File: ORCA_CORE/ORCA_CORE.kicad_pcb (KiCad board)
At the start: 4 copper layers, 73 x 134.1 mm, 183 parts, among them J1 data_line_power, J10 Raspberry_Pi_2_3, J11 I2C, J12 I2C, J13 6Vout, J15 Conn_01x05_Pin, J16 Conn_01x05_Pin, J17 Vin_motor, J18 data_line_power, J19 +5Vin_cpu, J2 I2C_power, J20 5Vout, J21 Conn_01x02, J3 Vout_motor, J4 emergence, J5 Vin_batt, J6 Vin_ex, J7 Vout_power2usp, J8 Vin_power2usp, J9 +5Vout_cpu, P1 USB_C_Plug_USB2.0, Q1 TJ60S04M3L, Q2 BSS138, Q3 BSS138, Q4 IRLML6402, Q5 TJ60S04M3L, Q6 BSS138, Q7 BSS138, Q8 BSS138, U1 LTC2301IMS, U10 HY2112, U11 AP64502, U12 TPS61230A__board, U13 FT230XS, U14 BNO055, U15 NJM78055DL1, U2 NJM78055DL1, U3 CN3058E, U4 RH1B-UDC6V, U5 TPH11006NL, U6 TPH11006NL, U7 NJW4860, U8 AZ1117-3.3, U9 FS8205

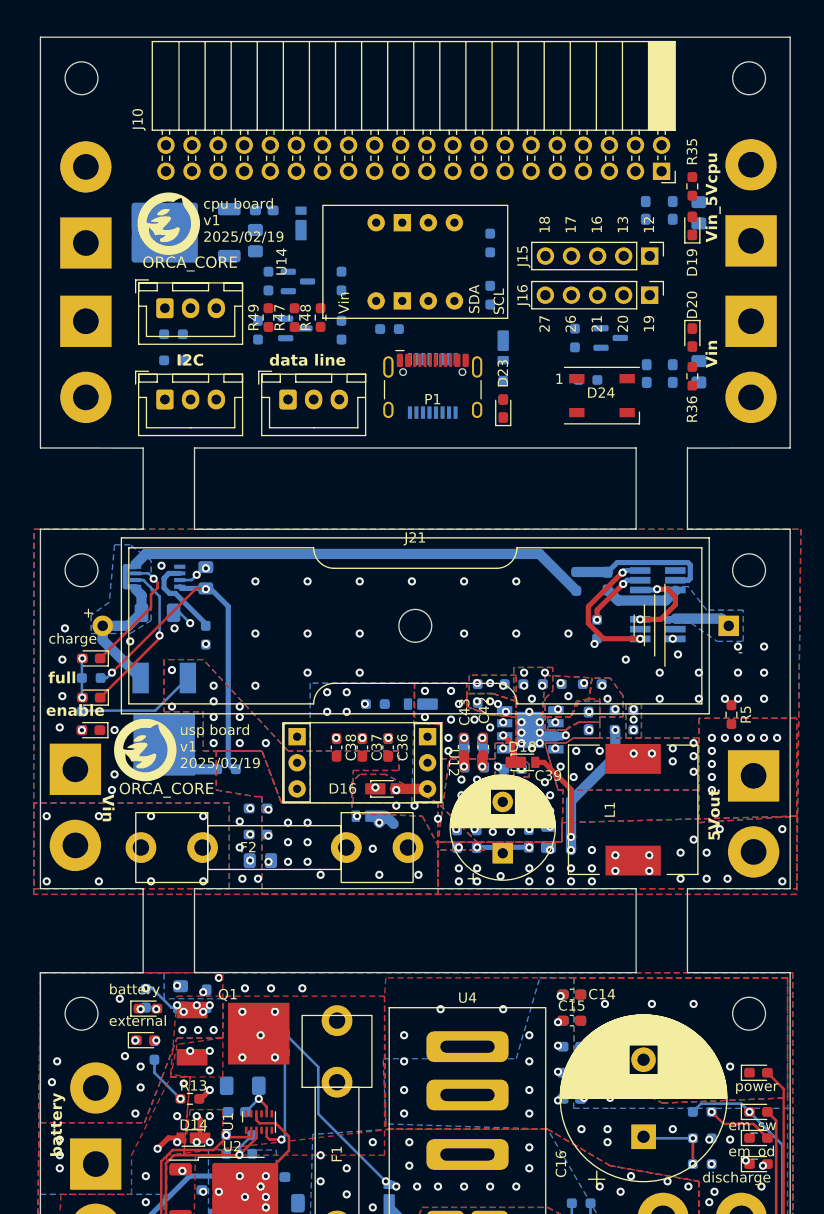
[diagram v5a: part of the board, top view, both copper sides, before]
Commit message: wired and filled all borad
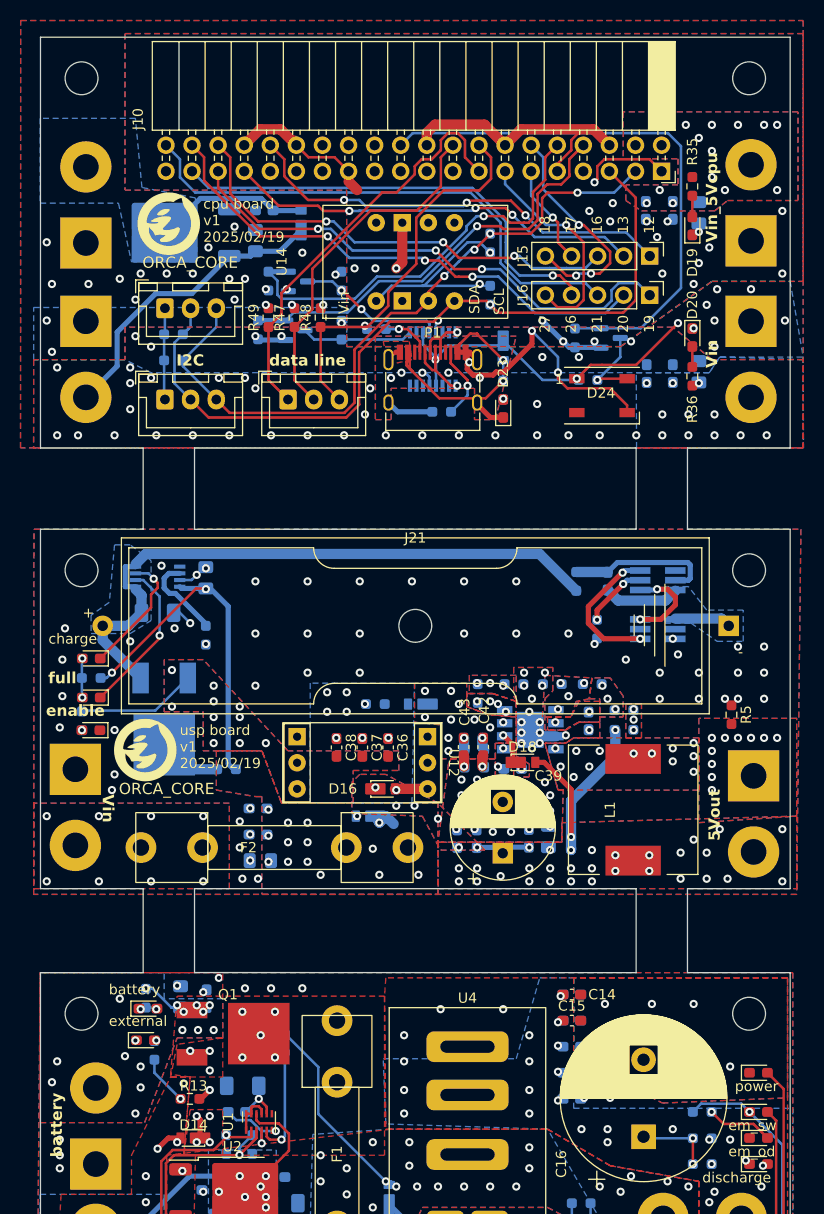
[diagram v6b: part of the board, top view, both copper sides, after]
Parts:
- added R51: 5.1k, Resistor_SMD:R_0603_1608Metric_Pad0.98x0.95mm_HandSolder, B.Cu at (132.4, 64.8)
- P1: value USB_C_Plug_USB2.0 -> USB_C_Receptacle_USB2.0; footprint Connector_USB:USB_C_Receptacle_HCTL_HC-TYPE-C-16P-01A_withmodel -> Conn:USB_C_Receptacle_XKB_U262-16XN-4BVC11
- moved U13 2.61 mm to (131.6, 59.6)
- moved R39 1.27 mm to (126.1, 56.7)
- moved P1 0.71 mm to (131.6, 62.8)
- moved Q6 0.18 mm to (118.2, 56.8)
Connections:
- D22 pad 2: Net-(D22-A) -> GND2
- P1 pad A4: Net-(D22-A) -> GND2
- P1 pad A6: Net-(P1-D+) -> Net-(U13-USBDP)
- P1 pad A7: Net-(P1-D-) -> Net-(U13-USBDM)
- P1 pad A8: (no net) -> unconnected-(P1-SBU1-PadA8)
- P1 pad A9: Net-(D22-A) -> GND2
- P1 pad B4: Net-(D22-A) -> GND2
- P1 pad B5: unconnected-(P1-VCONN-PadB5) -> Net-(P1-CC2)
- P1 pad B6: (no net) -> Net-(U13-USBDP)
- P1 pad B7: (no net) -> Net-(U13-USBDM)
- P1 pad B8: (no net) -> unconnected-(P1-SBU2-PadB8)
- P1 pad B9: Net-(D22-A) -> GND2
- R40 pad 1: Net-(D22-A) -> GND2
- U13 pad 8: Net-(P1-D+) -> Net-(U13-USBDP)
- U13 pad 9: Net-(P1-D-) -> Net-(U13-USBDM)
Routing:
- net GND2: track 0.00 -> 137.6 mm, vias 0 -> 30
- net SCL: track 0.00 -> 76.5 mm, vias 0 -> 1
- net SDA: track 0.00 -> 68.0 mm, vias 0 -> 4
- net +3V3_cpu: track 0.00 -> 58.4 mm, vias 0 -> 9
- net full_color_led_3V3: track 0.00 -> 54.1 mm
- net /cpu/GPIO21: track 0.00 -> 51.4 mm
- net /cpu/GPIO20: track 0.00 -> 50.9 mm, vias 0 -> 3
- net +5V_cpu: track 0.00 -> 50.7 mm, vias 0 -> 19
- net /cpu/GPIO19: track 0.00 -> 50.6 mm, vias 0 -> 3
- net /cpu/GPIO26: track 0.00 -> 44.7 mm, vias 0 -> 1
- net /cpu/GPIO16: track 0.00 -> 44.6 mm, vias 0 -> 3
- net /cpu/GPIO12: track 0.00 -> 43.2 mm, vias 0 -> 3
- net RXD_3V3: track 0.00 -> 41.7 mm, vias 0 -> 1
- net TXD_3V3: track 0.00 -> 41.4 mm, vias 0 -> 1
- net /cpu/emerg_detector: track 0.00 -> 40.9 mm
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- added copper zone on In1.Cu, net +3V3_cpu
- added copper zone on B.Cu, net +5V_cpu
- added copper zone on F.Cu, net +5V_cpu
- added copper zone on In1.Cu, net +5V_cpu
- added copper zone on In2.Cu, net +5V_cpu
- added copper zone on B.Cu, net +5V_cpu2servo
- added copper zone on In1.Cu, net +5V_cpu2servo
- added copper zone on B.Cu, net +6V_cpu
- added copper zone on F.Cu, net +6V_cpu
- added copper zone on In1.Cu, net +6V_cpu
- added copper zone on B.Cu, net GND2
- added copper zone on F.Cu, net GND2
- added copper zone on In2.Cu, net GND2

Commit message: solv errors waiting check
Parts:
- moved R48 5.08 mm to (115.6, 55.6)
- moved R49 5.08 mm to (120.7, 55.6)
- moved J12 5.00 mm to (110.5, 63.8), turned to 180 degrees
- moved J18 4.95 mm to (122.4, 63.6), turned to 180 degrees
- moved J11 4.92 mm to (110.4, 54.7), turned to 180 degrees
- moved R37 3.00 mm to (109.3, 57.2), turned to 180 degrees
- moved R38 3.00 mm to (109.3, 59.8), turned to 180 degrees
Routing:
- net /cpu/emerg_detector: track 40.9 -> 32.7 mm
- net GND: track 53.9 -> 46.7 mm, vias 191 -> 202
- net SDA: track 68.0 -> 74.9 mm
- net GND2: track 137.6 -> 132.4 mm, vias 30 -> 50
- net /cpu/emerge_order: track 37.6 -> 41.9 mm
- net +3V3_cpu: track 58.4 -> 61.8 mm
- net /cpu/power_checker: track 34.6 -> 33.9 mm
